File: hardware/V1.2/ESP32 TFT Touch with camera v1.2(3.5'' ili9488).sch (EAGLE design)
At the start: 99 parts, among them IC1 CP2104, P2 AFC01-S06FCC-00, P3 AFC01-S06FCC-00, P5 FPC-40P, Q2 AO3400, Q3 S8050, Q4 S8050, Q5 S8050, U2 ESP32-WROVER, U4 LD1117/3.3v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

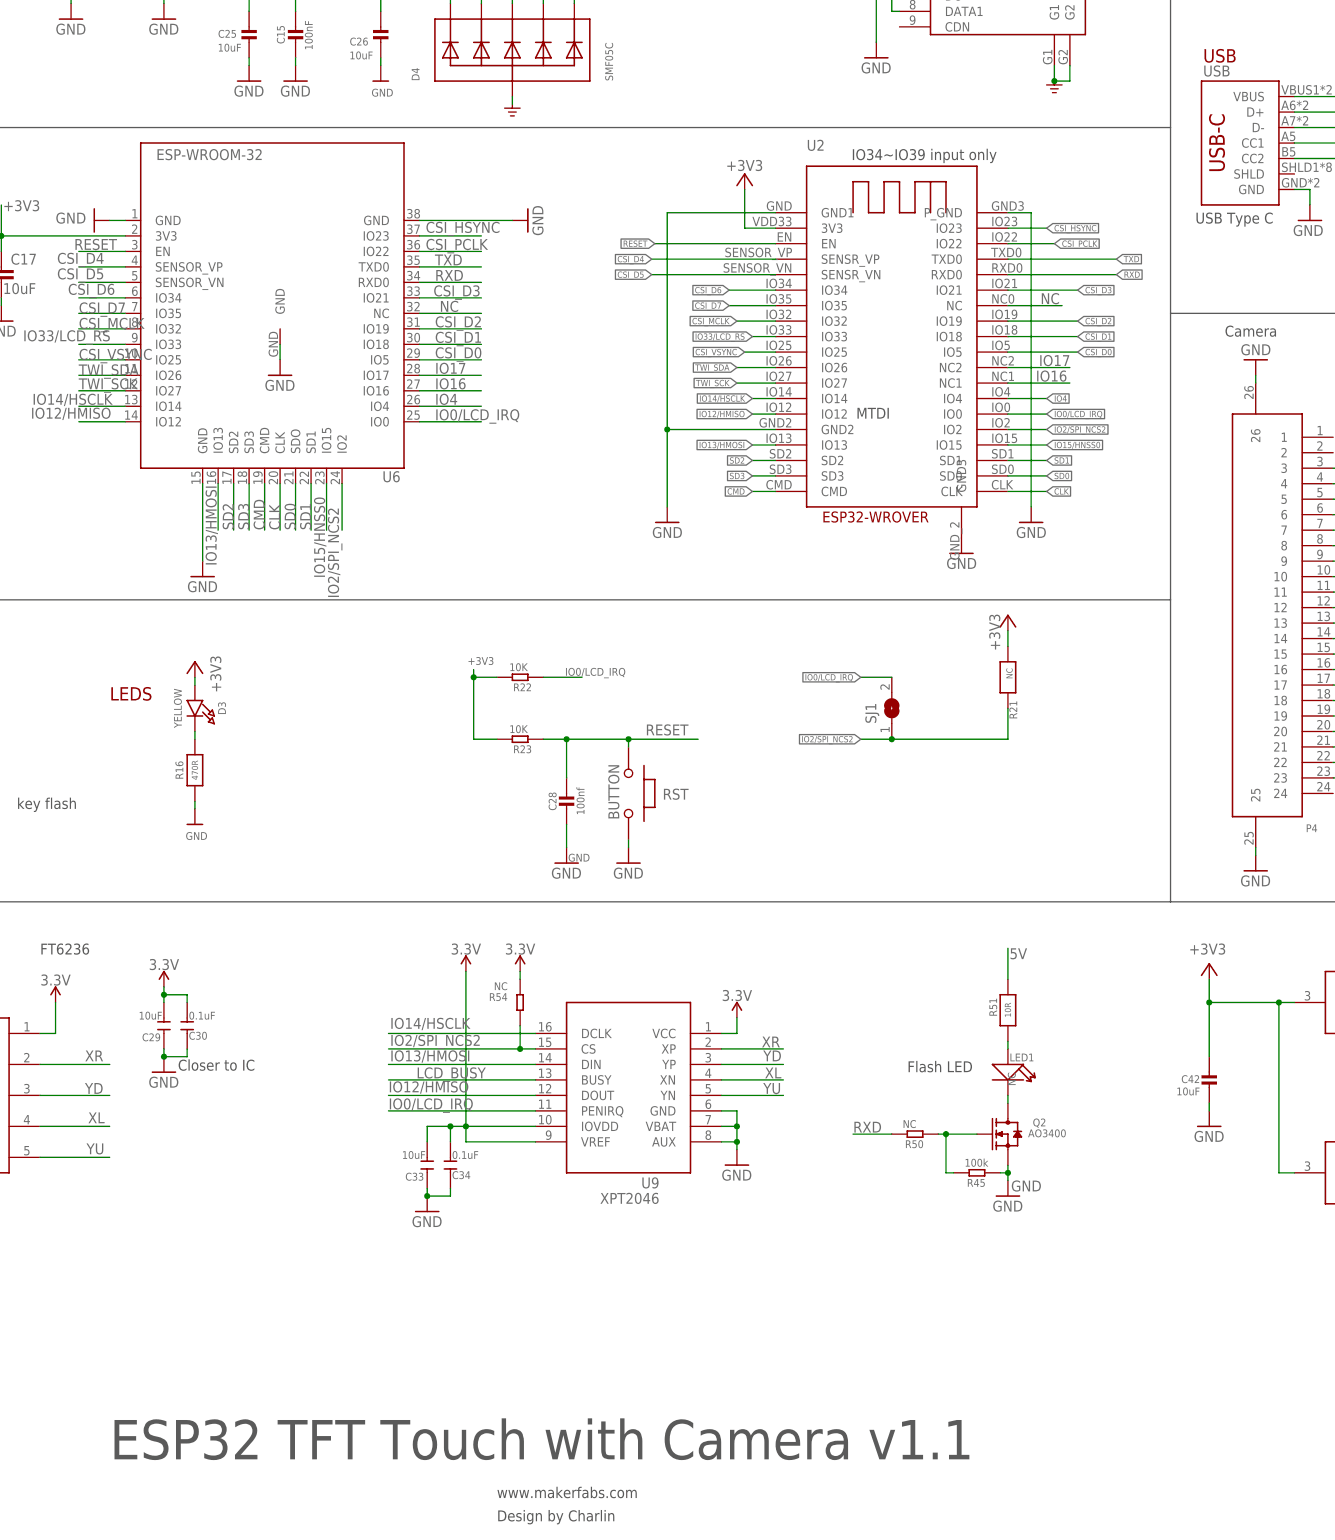
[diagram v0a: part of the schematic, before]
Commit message: change SCH to V1.2
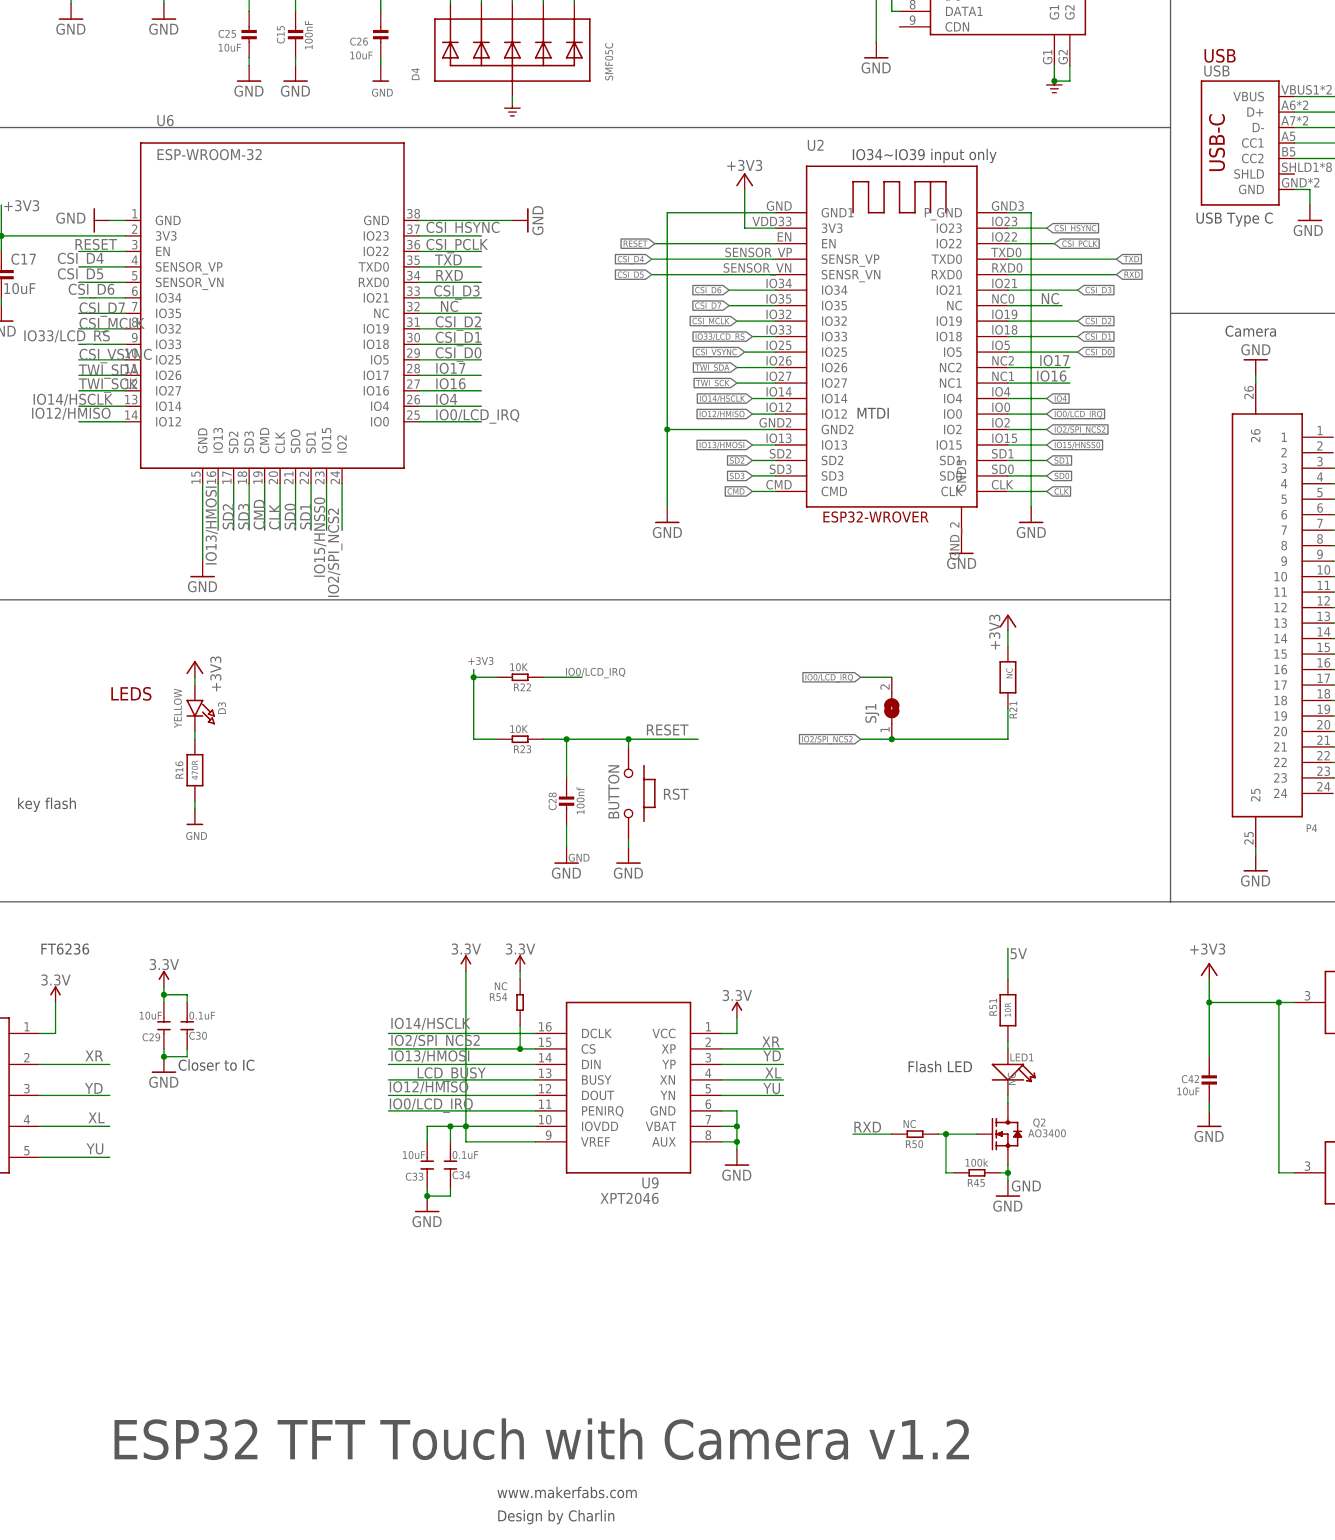
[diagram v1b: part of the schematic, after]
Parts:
- U6: device esp32:ESP-WROOM-32 -> ESP32:ESP-WROOM-32
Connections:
- net GND: no longer U6.GND
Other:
- note added: "ESP32 TFT Touch with Camera v1.2"
- note removed: "ESP32 TFT Touch with Camera v1.1"
